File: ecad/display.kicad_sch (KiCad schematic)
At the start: 51 parts, among them Q1 2N7002, Q10 BSS84, Q11 BSS84, Q13 BSS84, Q2 2N7002, Q3 2N7002, Q4 2N7002, Q5 BSS84, Q6 BSS84, Q7 BSS84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

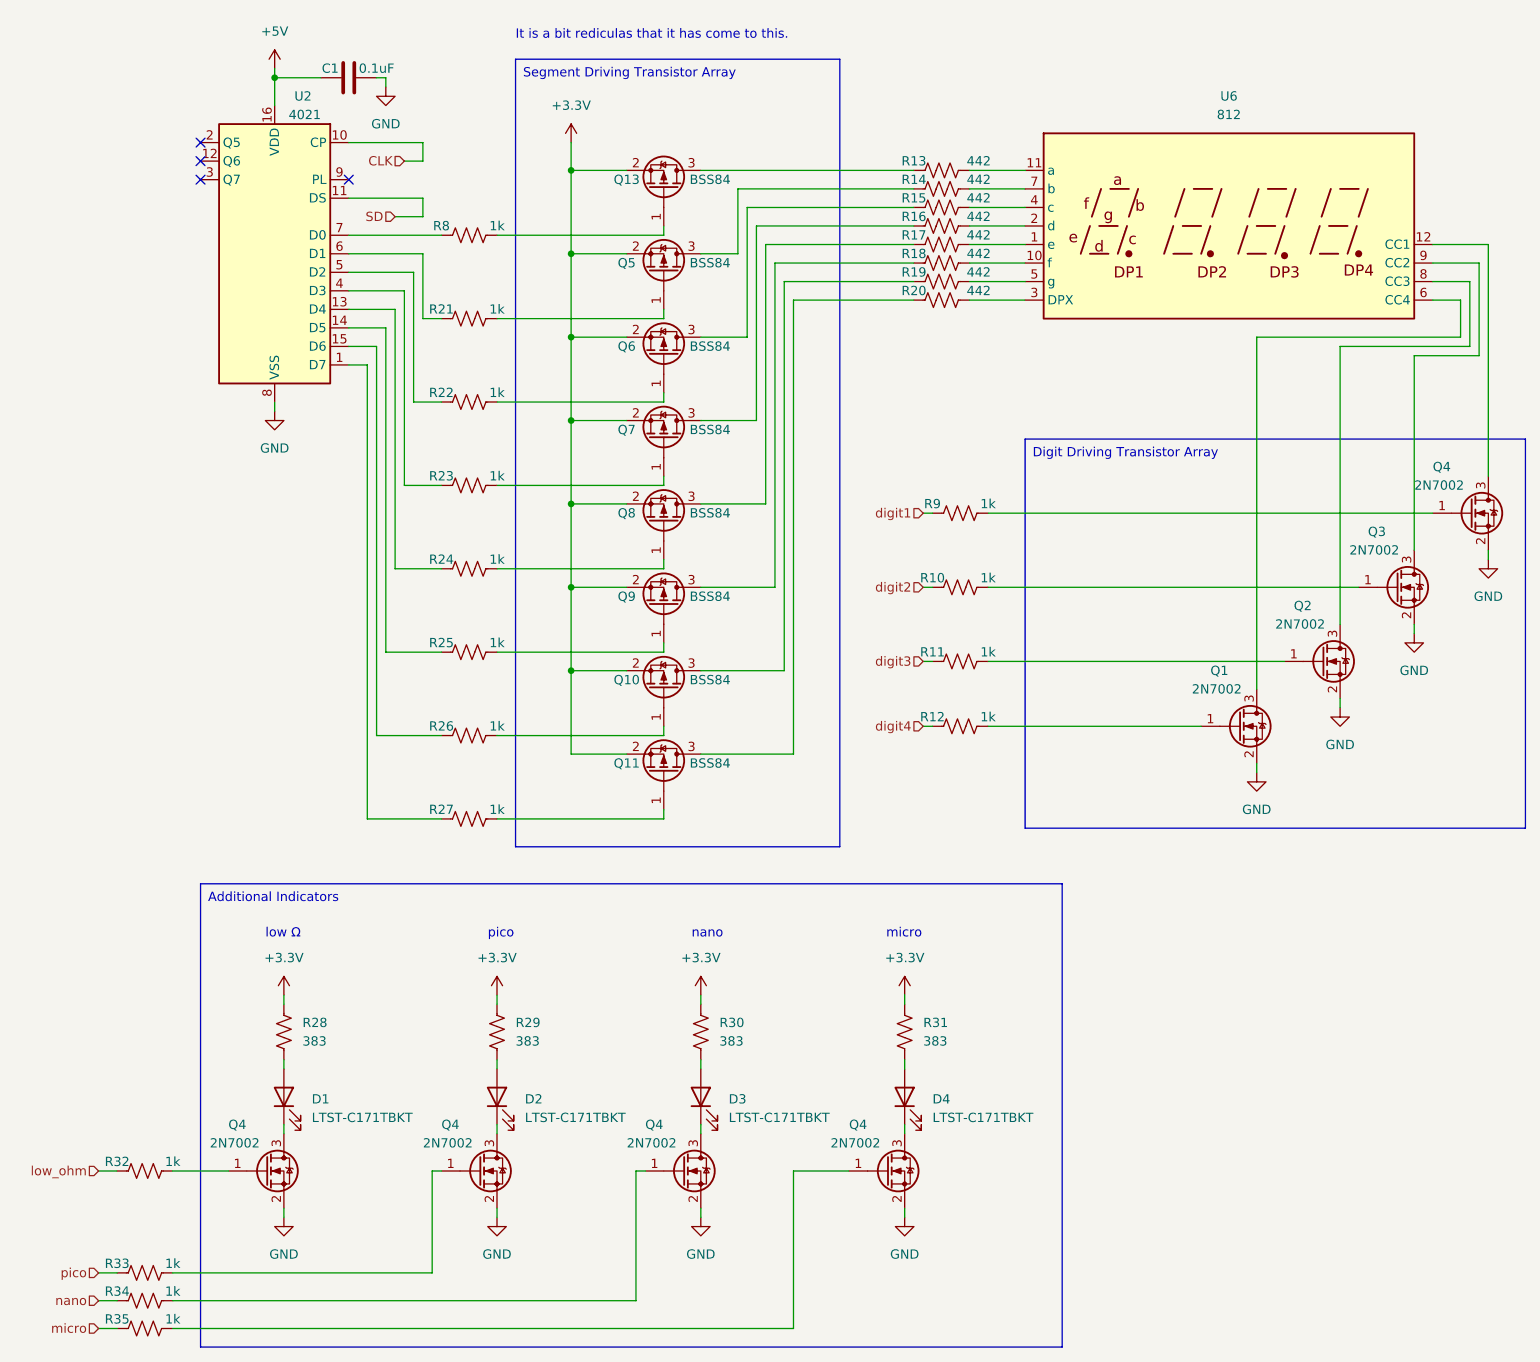
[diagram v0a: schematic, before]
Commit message: cap interpolation test
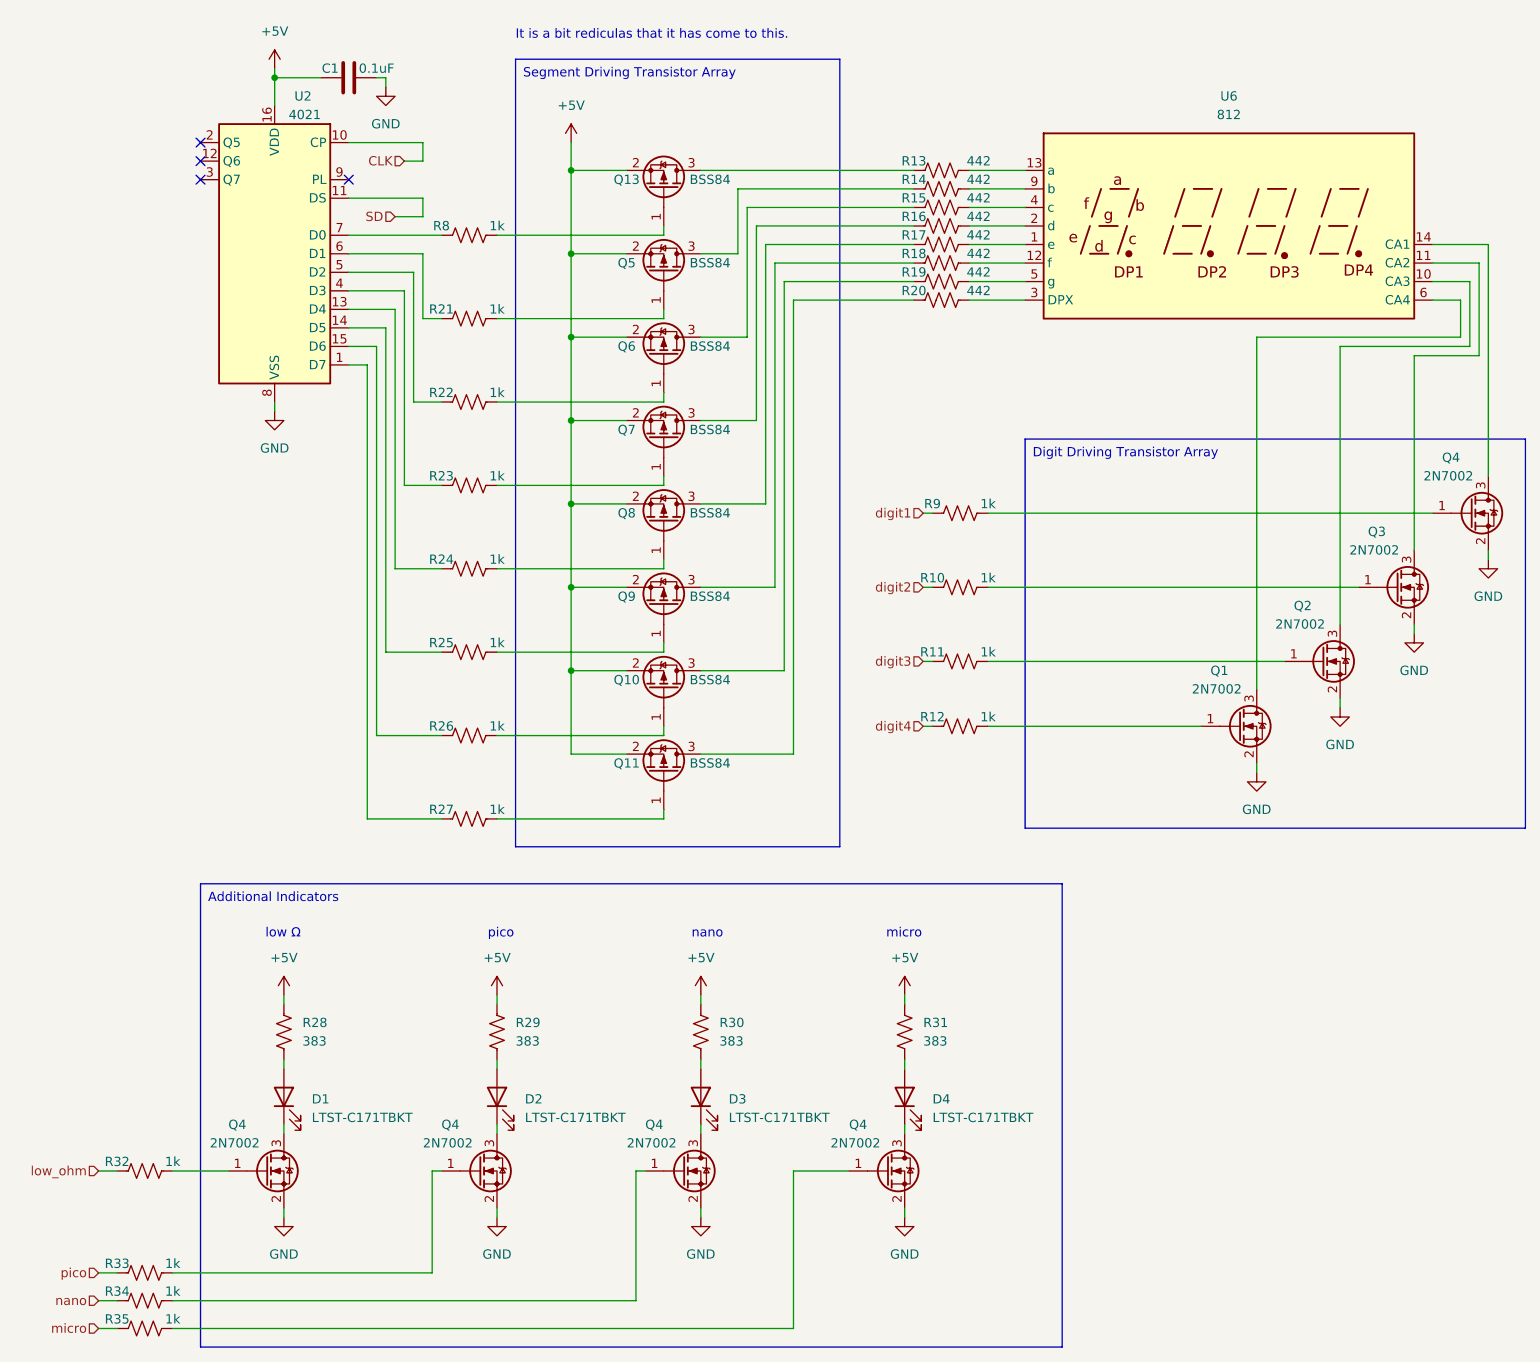
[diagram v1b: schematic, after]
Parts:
- removed U6: 812, Display_7Segment:CA56-12EWA, symbol Display_Character:CC56-12EWA
- added U6: 812, Display_7Segment:CA56-12EWA, symbol multimeter_parts:812
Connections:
- net +3.3V is gone; now on net +5V: Q10.2 (S), Q11.2 (S), Q13.2 (S), Q5.2 (S), Q6.2 (S), Q7.2 (S), Q8.2 (S), Q9.2 (S), R28.1, R29.1, R30.1, R31.1
- net at R17.2: now also U6.1 (e)
- net at Q4.3 (D): now also U6.14 (CA1)
- net at Q2.3 (D): now also U6.10 (CA3)
- net at R18.2: now also U6.12 (f)
- net at R20.2: now also U6.3 (DPX)
- net at R13.2: now also U6.13 (a)
- net at R16.2: now also U6.2 (d)
- net at R19.2: now also U6.5 (g)
- net at Q1.3 (D): now also U6.6 (CA4)
- net at R14.2: now also U6.9 (b)
- net at R15.2: now also U6.4 (c)
- net at Q3.3 (D): now also U6.11 (CA2)

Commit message: layout finished
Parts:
- removed U6: 812, Display_7Segment:CA56-12EWA, symbol multimeter_parts:812
- added U4: CC56-12SURKWA, Display_7Segment:CA56-12SURKWA, symbol Display_Character:CC56-12SURKWA
- C1: Digikey Part # (none) -> 1276-1003-1-ND; Part # (none) -> CL21B104KBCNNNC; Unit Price (none) -> 0.1
- D1, D2, D3, D4: value LTST-C171TBKT -> LTST-C170KRKT; Digikey Part # (none) -> 160-1415-1-ND; Part # (none) -> LTST-C170KRKT; Unit Price (none) -> 0.32
- Q1, Q2, Q3, Q4: Digikey Part # (none) -> 2N7002NCT-ND; Part # (none) -> 2N7002; Unit Price (none) -> 0.45
- Q10, Q11, Q13, Q5, Q6, Q7, Q8, Q9: Digikey Part # (none) -> 4786-BSS84CT-ND; Part # (none) -> BSS84; Unit Price (none) -> 0.15
- R10, R11, R12, R21, R22, R23, R24, R25, R26, R27, R32, R33, R34, R35, R8, R9: Digikey Part # (none) -> RMCF0805FT1K00CT-ND; Part # (none) -> RMCF0805FT1K00; Unit Price (none) -> 0.1
- R13, R14, R15, R16, R17, R18, R19, R20: value 442 -> 649; Digikey Part # (none) -> RMCF0805FT649RCT-ND; Part # (none) -> RMCF0805FT649R; Unit Price (none) -> 0.1
- R28, R29, R30, R31: value 383 -> 649; Digikey Part # (none) -> RMCF0805FT649RCT-ND; Part # (none) -> RMCF0805FT649R; Unit Price (none) -> 0.1
- U2: Digikey Part # (none) -> 296-38905-1-ND; Part # (none) -> CD4021BM96; Unit Price (none) -> 0.54
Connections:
- net at R17.2: now also U4.1 (e)
- net at Q2.3 (D): now also U4.8 (CC3)
- net at Q3.3 (D): now also U4.9 (CC2)
- net at R18.2: now also U4.10 (f)
- net at R13.2: now also U4.11 (a)
- net at Q4.3 (D): now also U4.12 (CC1)
- net at R16.2: now also U4.2 (d)
- net at R20.2: now also U4.3 (DPX)
- net at R15.2: now also U4.4 (c)
- net at R19.2: now also U4.5 (g)
- net at Q1.3 (D): now also U4.6 (CC4)
- net at R14.2: now also U4.7 (b)
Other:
- note added: "Somehow, it has come to this ..."
- note removed: "It is a bit rediculas that it has come to this."
- moved on the sheet: R10, R11, R12, R9
